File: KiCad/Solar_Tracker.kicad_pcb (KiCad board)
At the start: 2 copper layers, 119.4 x 87.6 mm, 120 parts, among them J1 +48V_IN, J10 AZJMP, J11 ELJMP, J12 AZ, J13 CONN_01X03, J2 HOLE, J3 HOLE, J4 EL, J5 HOLE, J6 HOLE, J7 CONN_01X05, J8 GPIO, J9 GPIO, Q1 BUK9M42-60E, Q2 BUK9M42-60E, Q3 BUK9M42-60E, Q4 BUK9M42-60E, Q5 BUK9M42-60E, Q6 BUK9M42-60E, Q7 BUK9M42-60E, Q8 BUK9M42-60E, U1 MER1S4805SC, U10 TLP291, U11 75LBC182, U12 A4927, U2 A4927, U3 Nano, U4 A4927, U5 A4927, U6 MER1S4805SC, U7 TLP291, U8 TLP291, U9 TLP291

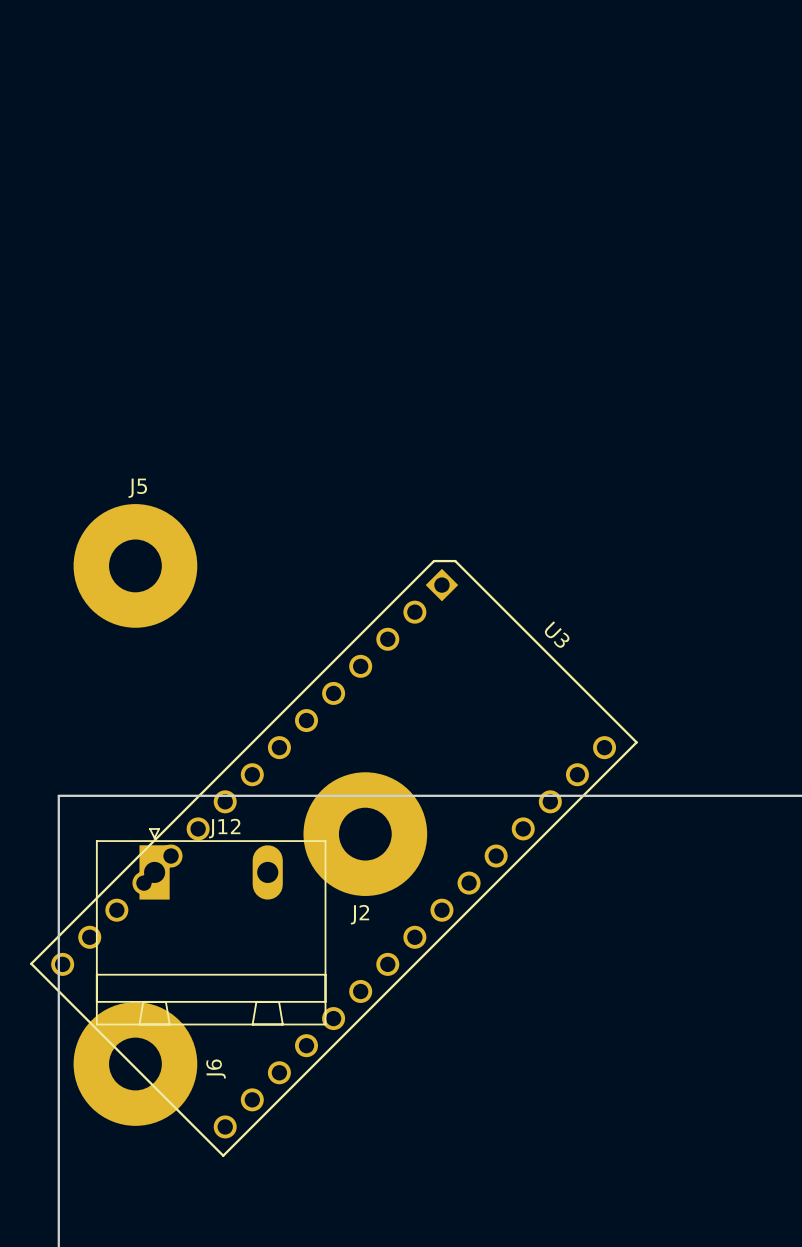
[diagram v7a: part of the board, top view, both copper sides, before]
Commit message: Updated netlist in pcb
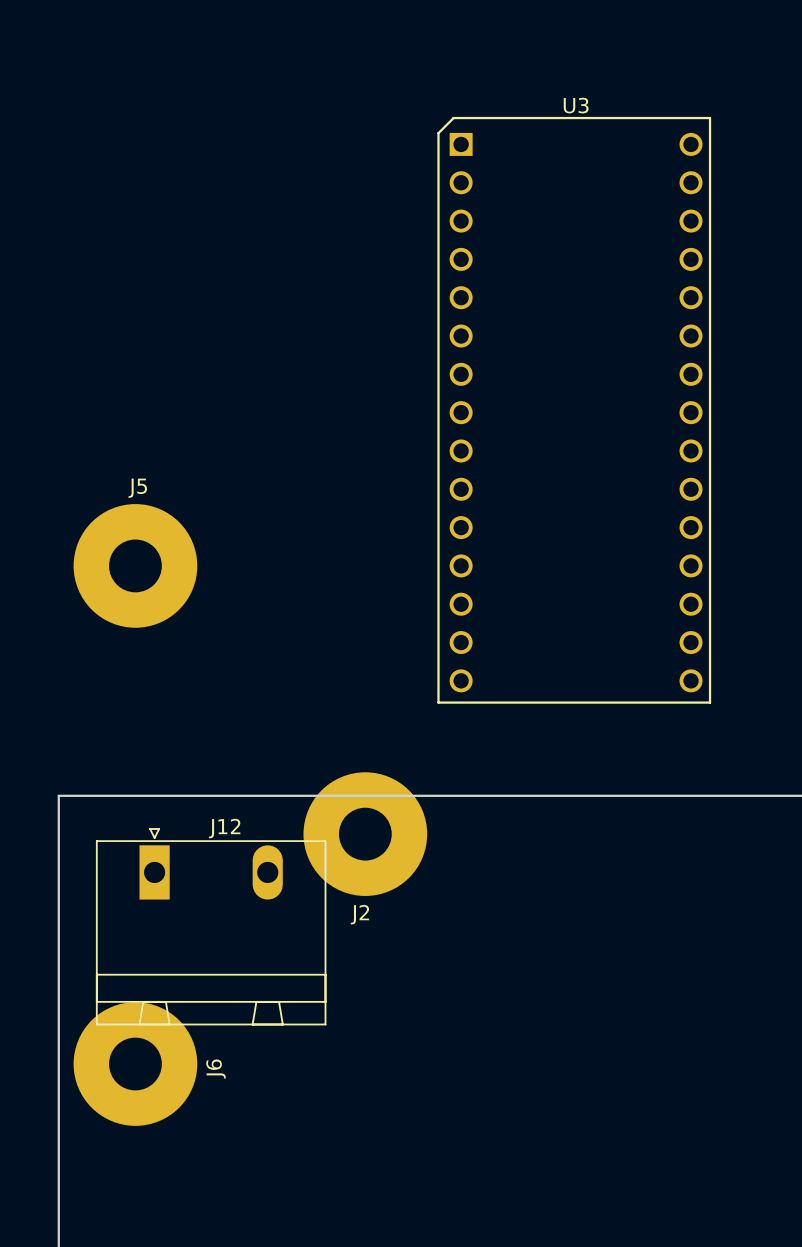
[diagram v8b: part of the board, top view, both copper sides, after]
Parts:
- moved U3 29.2 mm to (39.4, -30.5), turned to 0 degrees
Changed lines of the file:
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@@
   )
   (module SOLAR_TRACKER:nano (layer F.Cu)
-    (at 38.1 -1.27 315)
-    (fp_text reference U3 (at 7.75 -3 315) (layer F.SilkS)
+    (at 39.37 -30.48)
+    (fp_text reference U3 (at 7.62 -2.54) (layer F.SilkS)
       (effects (font (size 1 1) (thickness 0.15)))
     )
-    (fp_text value Nano (at 7.25 37.75 315) (layer F.Fab)
+    (fp_text value Nano (at 7.25 37.75) (layer F.Fab)
       (effects (font (size 1 1) (thickness 0.15)))
     )
@@
     (fp_line (start 16.5 -1.75) (end 16.5 37) (layer F.SilkS) (width 0.15))
     (fp_line (start 16.5 37) (end -1.5 37) (layer F.SilkS) (width 0.15))
-    (pad 1 thru_hole rect (at 0 0 315) (size 1.524 1.524) (drill 1.016) (layers *.Cu *.Mask)
+    (pad 1 thru_hole rect (at 0 0) (size 1.524 1.524) (drill 1.016) (layers *.Cu *.Mask)
       (net 44 TX))
-    (pad 2 thru_hole circle (at 0 2.54 315) (size 1.524 1.524) (drill 1.016) (layers *.Cu *.Mask)
+    (pad 2 thru_hole circle (at 0 2.54) (size 1.524 1.524) (drill 1.016) (layers *.Cu *.Mask)
       (net 42 RX))
-    (pad 3 thru_hole circle (at 0 5.08 315) (size 1.524 1.524) (drill 1.016) (layers *.Cu *.Mask)
+    (pad 3 thru_hole circle (at 0 5.08) (size 1.524 1.524) (drill 1.016) (layers *.Cu *.Mask)
       (net 133 "Net-(U3-Pad3)"))
-    (pad 4 thru_hole circle (at 0 7.62 315) (size 1.524 1.524) (drill 1.016) (layers *.Cu *.Mask)
+    (pad 4 thru_hole circle (at 0 7.62) (size 1.524 1.524) (drill 1.016) (layers *.Cu *.Mask)
       (net 1 Earth))
-    (pad 5 thru_hole circle (at 0 10.16 315) (size 1.524 1.524) (drill 1.016) (layers *.Cu *.Mask)
+    (pad 5 thru_hole circle (at 0 10.16) (size 1.524 1.524) (drill 1.016) (layers *.Cu *.Mask)
       (net 134 AZBH))
-    (pad 6 thru_hole circle (at 0 12.7 315) (size 1.524 1.524) (drill 1.016) (layers *.Cu *.Mask)
+    (pad 6 thru_hole circle (at 0 12.7) (size 1.524 1.524) (drill 1.016) (layers *.Cu *.Mask)
       (net 135 AZBL))
-    (pad 7 thru_hole circle (at 0 15.24 315) (size 1.524 1.524) (drill 1.016) (layers *.Cu *.Mask)
+    (pad 7 thru_hole circle (at 0 15.24) (size 1.524 1.524) (drill 1.016) (layers *.Cu *.Mask)
       (net 136 AZFH))
-    (pad 8 thru_hole circle (at 0 17.78 315) (size 1.524 1.524) (drill 1.016) (layers *.Cu *.Mask)
+    (pad 8 thru_hole circle (at 0 17.78) (size 1.524 1.524) (drill 1.016) (layers *.Cu *.Mask)
       (net 137 AZFL))
-    (pad 9 thru_hole circle (at 0 20.32 315) (size 1.524 1.524) (drill 1.016) (layers *.Cu *.Mask)
+    (pad 9 thru_hole circle (at 0 20.32) (size 1.524 1.524) (drill 1.016) (layers *.Cu *.Mask)
       (net 43 EN))
-    (pad 10 thru_hole circle (at 0 22.86 315) (size 1.524 1.524) (drill 1.016) (layers *.Cu *.Mask)
+    (pad 10 thru_hole circle (at 0 22.86) (size 1.524 1.524) (drill 1.016) (layers *.Cu *.Mask)
       (net 46 ISO_PWR_DET))
-    (pad 11 thru_hole circle (at 0 25.4 315) (size 1.524 1.524) (drill 1.016) (layers *.Cu *.Mask)
+    (pad 11 thru_hole circle (at 0 25.4) (size 1.524 1.524) (drill 1.016) (layers *.Cu *.Mask)
       (net 131 ELBH))
-    (pad 12 thru_hole circle (at 0 27.94 315) (size 1.524 1.524) (drill 1.016) (layers *.Cu *.Mask)
+    (pad 12 thru_hole circle (at 0 27.94) (size 1.524 1.524) (drill 1.016) (layers *.Cu *.Mask)
       (net 132 ELBL))
-    (pad 13 thru_hole circle (at 0 30.48 315) (size 1.524 1.524) (drill 1.016) (layers *.Cu *.Mask)
+    (pad 13 thru_hole circle (at 0 30.48) (size 1.524 1.524) (drill 1.016) (layers *.Cu *.Mask)
       (net 138 ELFH))
-    (pad 14 thru_hole circle (at 0 33.02 315) (size 1.524 1.524) (drill 1.016) (layers *.Cu *.Mask)
+    (pad 14 thru_hole circle (at 0 33.02) (size 1.524 1.524) (drill 1.016) (layers *.Cu *.Mask)
       (net 139 ELFL))
-    (pad 15 thru_hole circle (at 0 35.56 315) (size 1.524 1.524) (drill 1.016) (layers *.Cu *.Mask)
+    (pad 15 thru_hole circle (at 0 35.56) (size 1.524 1.524) (drill 1.016) (layers *.Cu *.Mask)
       (net 26 AZRTE))
-    (pad 16 thru_hole circle (at 15.24 35.56 315) (size 1.524 1.524) (drill 1.016) (layers *.Cu *.Mask)
+    (pad 16 thru_hole circle (at 15.24 35.56) (size 1.524 1.524) (drill 1.016) (layers *.Cu *.Mask)
       (net 27 ELRTE))
-    (pad 17 thru_hole circle (at 15.24 33.02 315) (size 1.524 1.524) (drill 1.016) (layers *.Cu *.Mask)
+    (pad 17 thru_hole circle (at 15.24 33.02) (size 1.524 1.524) (drill 1.016) (layers *.Cu *.Mask)
       (net 66 "Net-(U3-Pad17)"))
-    (pad 18 thru_hole circle (at 15.24 30.48 315) (size 1.524 1.524) (drill 1.016) (layers *.Cu *.Mask)
+    (pad 18 thru_hole circle (at 15.24 30.48) (size 1.524 1.524) (drill 1.016) (layers *.Cu *.Mask)
       (net 2 "Net-(C2-Pad1)"))
-    (pad 19 thru_hole circle (at 15.24 27.94 315) (size 1.524 1.524) (drill 1.016) (layers *.Cu *.Mask)
+    (pad 19 thru_hole circle (at 15.24 27.94) (size 1.524 1.524) (drill 1.016) (layers *.Cu *.Mask)
       (net 112 C0))
-    (pad 20 thru_hole circle (at 15.24 25.4 315) (size 1.524 1.524) (drill 1.016) (layers *.Cu *.Mask)
+    (pad 20 thru_hole circle (at 15.24 25.4) (size 1.524 1.524) (drill 1.016) (layers *.Cu *.Mask)
       (net 111 C1))
-    (pad 21 thru_hole circle (at 15.24 22.86 315) (size 1.524 1.524) (drill 1.016) (layers *.Cu *.Mask)
+    (pad 21 thru_hole circle (at 15.24 22.86) (size 1.524 1.524) (drill 1.016) (layers *.Cu *.Mask)
       (net 110 C2))
-    (pad 22 thru_hole circle (at 15.24 20.32 315) (size 1.524 1.524) (drill 1.016) (layers *.Cu *.Mask)
+    (pad 22 thru_hole circle (at 15.24 20.32) (size 1.524 1.524) (drill 1.016) (layers *.Cu *.Mask)
       (net 109 C3))
-    (pad 23 thru_hole circle (at 15.24 17.78 315) (size 1.524 1.524) (drill 1.016) (layers *.Cu *.Mask)
+    (pad 23 thru_hole circle (at 15.24 17.78) (size 1.524 1.524) (drill 1.016) (layers *.Cu *.Mask)
       (net 117 TLED))
-    (pad 24 thru_hole circle (at 15.24 15.24 315) (size 1.524 1.524) (drill 1.016) (layers *.Cu *.Mask)
+    (pad 24 thru_hole circle (at 15.24 15.24) (size 1.524 1.524) (drill 1.016) (layers *.Cu *.Mask)
       (net 115 RLED))
-    (pad 25 thru_hole circle (at 15.24 12.7 315) (size 1.524 1.524) (drill 1.016) (layers *.Cu *.Mask)
+    (pad 25 thru_hole circle (at 15.24 12.7) (size 1.524 1.524) (drill 1.016) (layers *.Cu *.Mask)
       (net 140 A6))
-    (pad 26 thru_hole circle (at 15.24 10.16 315) (size 1.524 1.524) (drill 1.016) (layers *.Cu *.Mask)
+    (pad 26 thru_hole circle (at 15.24 10.16) (size 1.524 1.524) (drill 1.016) (layers *.Cu *.Mask)
       (net 141 A7))
-    (pad 27 thru_hole circle (at 15.24 7.62 315) (size 1.524 1.524) (drill 1.016) (layers *.Cu *.Mask)
+    (pad 27 thru_hole circle (at 15.24 7.62) (size 1.524 1.524) (drill 1.016) (layers *.Cu *.Mask)
       (net 142 "Net-(U3-Pad27)"))
-    (pad 28 thru_hole circle (at 15.24 5.08 315) (size 1.524 1.524) (drill 1.016) (layers *.Cu *.Mask)
+    (pad 28 thru_hole circle (at 15.24 5.08) (size 1.524 1.524) (drill 1.016) (layers *.Cu *.Mask)
       (net 143 "Net-(U3-Pad28)"))
-    (pad 29 thru_hole circle (at 15.24 2.54 315) (size 1.524 1.524) (drill 1.016) (layers *.Cu *.Mask)
+    (pad 29 thru_hole circle (at 15.24 2.54) (size 1.524 1.524) (drill 1.016) (layers *.Cu *.Mask)
       (net 1 Earth))
-    (pad 30 thru_hole circle (at 15.24 0 315) (size 1.524 1.524) (drill 1.016) (layers *.Cu *.Mask)
+    (pad 30 thru_hole circle (at 15.24 0) (size 1.524 1.524) (drill 1.016) (layers *.Cu *.Mask)
       (net 6 +5V))
   )
